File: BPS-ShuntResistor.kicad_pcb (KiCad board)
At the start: 2 copper layers, 40.1 x 35.1 mm, 15 parts, among them J3 Amp_Conn

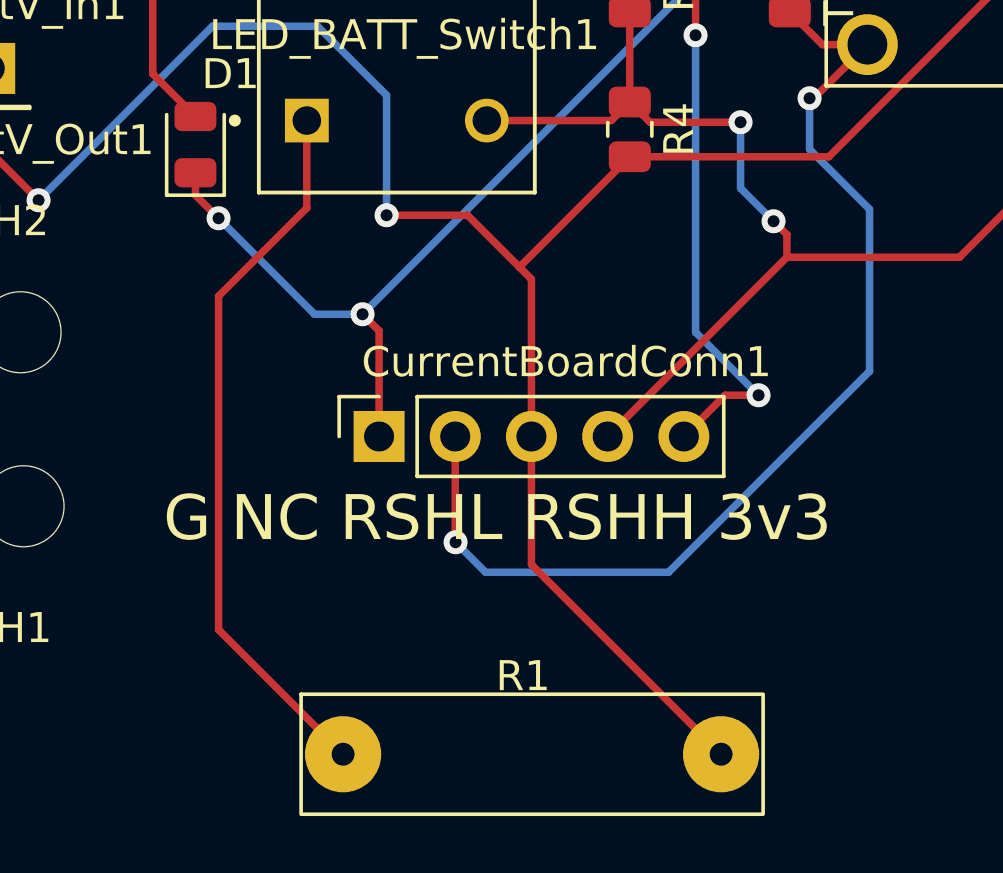
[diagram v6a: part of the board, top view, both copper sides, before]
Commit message: Updated BOM csv with approximate prices and potential Mouser lists
Ignore PCB update, footprint for 1x5 connector not decided
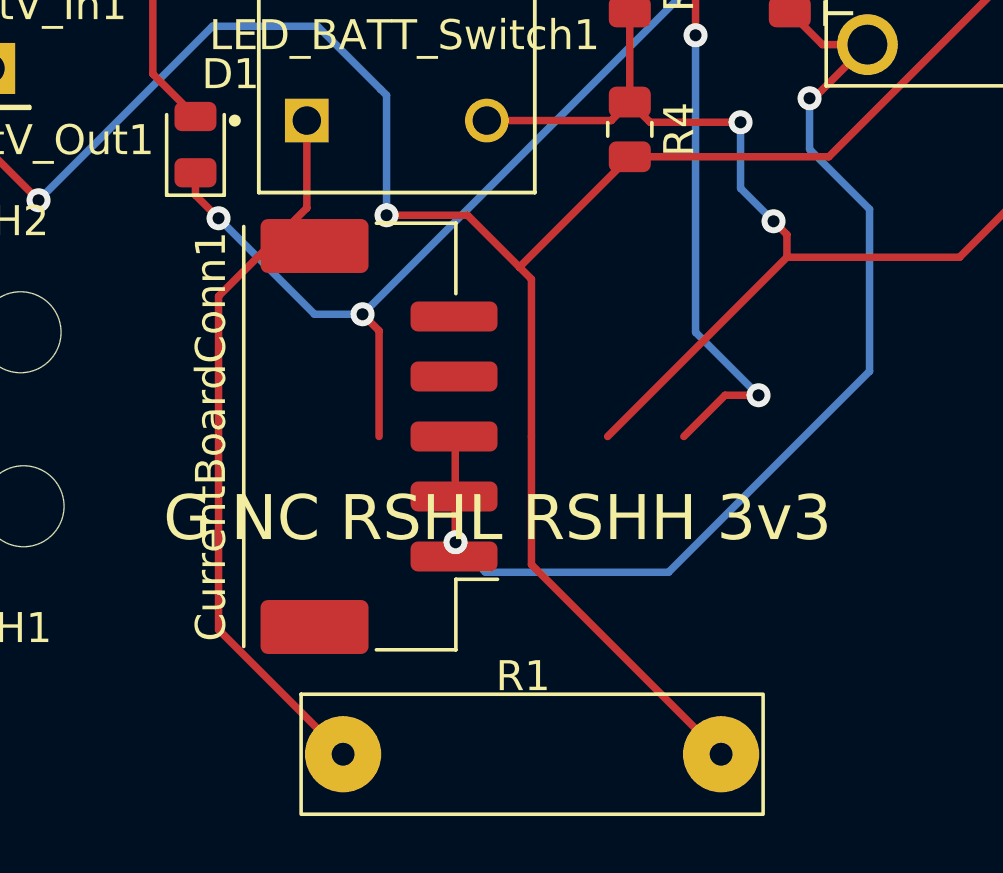
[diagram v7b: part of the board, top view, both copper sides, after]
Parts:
- CurrentBoardConn1: value Conn_01x05_Female -> Conn_01x05_Male; footprint Connector_PinSocket_2.54mm:PinSocket_1x05_P2.54mm_Vertical -> Connector_Molex:Molex_CLIK-Mate_502443-0570_1x05-1MP_P2.00mm_Vertical
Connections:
- CurrentBoardConn1 pad 1: GND -> ETS
- CurrentBoardConn1 pad 2: ETS -> RSHL
- CurrentBoardConn1 pad 3: RSHL -> RSHH
- CurrentBoardConn1 pad 4: RSHH -> +3V3
- CurrentBoardConn1 pad 5: +3V3 -> GND
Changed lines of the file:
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@@
   (net 4 "RSHL")
   (net 5 "RSHH")
-  (net 6 "Net-(R1-Pad1)")
-  (net 7 "Net-(R2-Pad2)")
+  (net 6 "Net-(LED_BATT_Switch1-Pad1)")
+  (net 7 "Net-(LED_BATT_Switch1-Pad3)")
   (net 8 "+3V3")
   (net 9 "Net-(R3-Pad1)")
@@
       (net 2 "Net-(D1-Pad2)") (pintype "passive"))
     (pad "2" smd roundrect (at 0.9125 0) (size 1.025 1.4) (layers "F.Cu" "F.Paste" "F.Mask") (roundrect_rratio 0.243902)
-      (net 7 "Net-(R2-Pad2)") (pintype "passive"))
+      (net 7 "Net-(LED_BATT_Switch1-Pad3)") (pintype "passive"))
     (model "${KICAD6_3DMODEL_DIR}/Resistor_SMD.3dshapes/R_0805_2012Metric.wrl"
       (offset (xyz 0 0 0))
@@
     (fp_circle (center -5.4 2.5) (end -5.3 2.5) (layer "F.Fab") (width 0.2) (fill none))
     (pad "1" thru_hole rect (at -3 2.5) (size 1.458 1.458) (drill 0.95) (layers *.Cu *.Mask)
-      (net 6 "Net-(R1-Pad1)") (pinfunction "1") (pintype "passive"))
+      (net 6 "Net-(LED_BATT_Switch1-Pad1)") (pinfunction "1") (pintype "passive"))
     (pad "2" thru_hole circle (at 3 2.5) (size 1.458 1.458) (drill 0.95) (layers *.Cu *.Mask)
       (net 5 "RSHH") (pinfunction "2") (pintype "passive"))
     (pad "3" thru_hole circle (at -3 -2.5) (size 1.458 1.458) (drill 0.95) (layers *.Cu *.Mask)
-      (net 7 "Net-(R2-Pad2)") (pinfunction "3") (pintype "passive"))
+      (net 7 "Net-(LED_BATT_Switch1-Pad3)") (pinfunction "3") (pintype "passive"))
     (pad "4" thru_hole circle (at 3 -2.5) (size 1.458 1.458) (drill 0.95) (layers *.Cu *.Mask)
       (net 8 "+3V3") (pinfunction "4") (pintype "passive"))
   )
-  (footprint "Connector_PinSocket_2.54mm:PinSocket_1x05_P2.54mm_Vertical" (layer "F.Cu")
+  (footprint "Connector_Molex:Molex_CLIK-Mate_502443-0570_1x05-1MP_P2.00mm_Vertical" (layer "F.Cu")
     (at 81.05 72.975 90)
-    (descr "Through hole straight socket strip, 1x05, 2.54mm pitch, single row (from Kicad 4.0.7), script generated")
-    (tags "Through hole socket strip THT 1x05 2.54mm single row")
-    (property "Sheetfile" "BPS-ShuntResistor.kicad_sch")
-    (property "Sheetname" "")
-    (attr through_hole)
-    (fp_text reference "CurrentBoardConn1" (at 2.475 6.25 180) (layer "F.SilkS")
-      (effects (font (size 1 1) (thickness 0.15)))
-    )
-    (fp_text value "Conn_01x05_Female" (at 0 12.93 90) (layer "F.Fab")
-      (effects (font (size 1 1) (thickness 0.15)))
-    )
-    (fp_text user "${REFERENCE}" (at 0 5.08) (layer "F.Fab")
-      (effects (font (size 1 1) (thickness 0.15)))
-    )
-    (fp_line (start 1.33 1.27) (end 1.33 11.49) (layer "F.SilkS") (width 0.12))
-    (fp_line (start -1.33 1.27) (end 1.33 1.27) (layer "F.SilkS") (width 0.12))
-    (fp_line (start 0 -1.33) (end 1.33 -1.33) (layer "F.SilkS") (width 0.12))
-    (fp_line (start 1.33 -1.33) (end 1.33 0) (layer "F.SilkS") (width 0.12))
-    (fp_line (start -1.33 1.27) (end -1.33 11.49) (layer "F.SilkS") (width 0.12))
-    (fp_line (start -1.33 11.49) (end 1.33 11.49) (layer "F.SilkS") (width 0.12))
-    (fp_line (start 1.75 -1.8) (end 1.75 11.9) (layer "F.CrtYd") (width 0.05))
-    (fp_line (start 1.75 11.9) (end -1.8 11.9) (layer "F.CrtYd") (width 0.05))
-    (fp_line (start -1.8 11.9) (end -1.8 -1.8) (layer "F.CrtYd") (width 0.05))
-    (fp_line (start -1.8 -1.8) (end 1.75 -1.8) (layer "F.CrtYd") (width 0.05))
-    (fp_line (start 1.27 -0.635) (end 1.27 11.43) (layer "F.Fab") (width 0.1))
-    (fp_line (start -1.27 11.43) (end -1.27 -1.27) (layer "F.Fab") (width 0.1))
-    (fp_line (start 1.27 11.43) (end -1.27 11.43) (layer "F.Fab") (width 0.1))
-    (fp_line (start -1.27 -1.27) (end 0.635 -1.27) (layer "F.Fab") (width 0.1))
-    (fp_line (start 0.635 -1.27) (end 1.27 -0.635) (layer "F.Fab") (width 0.1))
-    (pad "1" thru_hole rect (at 0 0 90) (size 1.7 1.7) (drill 1) (layers *.Cu *.Mask)
-      (net 1 "GND") (pinfunction "Pin_1") (pintype "passive"))
-    (pad "2" thru_hole oval (at 0 2.54 90) (size 1.7 1.7) (drill 1) (layers *.Cu *.Mask)
-      (net 3 "ETS") (pinfunction "Pin_2") (pintype "passive"))
-    (pad "3" thru_hole oval (at 0 5.08 90) (size 1.7 1.7) (drill 1) (layers *.Cu *.Mask)
-      (net 4 "RSHL") (pinfunction "Pin_3") (pintype "passive"))
-    (pad "4" thru_hole oval (at 0 7.62 90) (size 1.7 1.7) (drill 1) (layers *.Cu *.Mask)
-      (net 5 "RSHH") (pinfunction "Pin_4") (pintype "passive"))
-    (pad "5" thru_hole oval (at 0 10.16 90) (size 1.7 1.7) (drill 1) (layers *.Cu *.Mask)
-      (net 8 "+3V3") (pinfunction "Pin_5") (pintype "passive"))
-    (model "${KICAD6_3DMODEL_DIR}/Connector_PinSocket_2.54mm.3dshapes/PinSocket_1x05_P2.54mm_Vertical.wrl"
+    (descr "Molex CLIK-Mate series connector, 502443-0570 (http://www.molex.com/pdm_docs/sd/5024430270_sd.pdf), generated with kicad-footprint-generator")
+    (tags "connector Molex CLIK-Mate side entry")
+    (property "Sheetfile" "BPS-ShuntResistor.kicad_sch")
+    (property "Sheetname" "")
+    (attr smd)
+    (fp_text reference "CurrentBoardConn1" (at 0 -5.6 90) (layer "F.SilkS")
+      (effects (font (size 1 1) (thickness 0.15)))
+    )
+    (fp_text value "Conn_01x05_Male" (at 0 5.15 90) (layer "F.Fab")
+      (effects (font (size 1 1) (thickness 0.15)))
+    )
+    (fp_text user "${REFERENCE}" (at 0 -0.98 90) (layer "F.Fab")
+      (effects (font (size 1 1) (thickness 0.15)))
+    )
+    (fp_line (start -4.76 2.56) (end -4.76 3.95) (layer "F.SilkS") (width 0.12))
+    (fp_line (start 7.11 -0.09) (end 7.11 2.56) (layer "F.SilkS") (width 0.12))
+    (fp_line (start 7.11 2.56) (end 4.76 2.56) (layer "F.SilkS") (width 0.12))
+    (fp_line (start -7.11 -0.09) (end -7.11 2.56) (layer "F.SilkS") (width 0.12))
+    (fp_line (start -7.11 2.56) (end -4.76 2.56) (layer "F.SilkS") (width 0.12))
+    (fp_line (start -7 -4.51) (end 7 -4.51) (layer "F.SilkS") (width 0.12))
+    (fp_line (start -7.75 -4.9) (end -7.75 4.45) (layer "F.CrtYd") (width 0.05))
+    (fp_line (start 7.75 4.45) (end 7.75 -4.9) (layer "F.CrtYd") (width 0.05))
+    (fp_line (start 7.75 -4.9) (end -7.75 -4.9) (layer "F.CrtYd") (width 0.05))
+    (fp_line (start -7.75 4.45) (end 7.75 4.45) (layer "F.CrtYd") (width 0.05))
+    (fp_line (start -7 -4.4) (end 7 -4.4) (layer "F.Fab") (width 0.1))
+    (fp_line (start -7 2.45) (end -7 -4.4) (layer "F.Fab") (width 0.1))
+    (fp_line (start -4.5 2.45) (end -4 1.742893) (layer "F.Fab") (width 0.1))
+    (fp_line (start 7 2.45) (end 7 -4.4) (layer "F.Fab") (width 0.1))
+    (fp_line (start -4 1.742893) (end -3.5 2.45) (layer "F.Fab") (width 0.1))
+    (fp_line (start -7 2.45) (end 7 2.45) (layer "F.Fab") (width 0.1))
+    (pad "1" smd roundrect (at -4 2.5 90) (size 1 2.9) (layers "F.Cu" "F.Paste" "F.Mask") (roundrect_rratio 0.25)
+      (net 3 "ETS") (pinfunction "Pin_1") (pintype "passive"))
+    (pad "2" smd roundrect (at -2 2.5 90) (size 1 2.9) (layers "F.Cu" "F.Paste" "F.Mask") (roundrect_rratio 0.25)
+      (net 4 "RSHL") (pinfunction "Pin_2") (pintype "passive"))
+    (pad "3" smd roundrect (at 0 2.5 90) (size 1 2.9) (layers "F.Cu" "F.Paste" "F.Mask") (roundrect_rratio 0.25)
+      (net 5 "RSHH") (pinfunction "Pin_3") (pintype "passive"))
+    (pad "4" smd roundrect (at 2 2.5 90) (size 1 2.9) (layers "F.Cu" "F.Paste" "F.Mask") (roundrect_rratio 0.25)
+      (net 8 "+3V3") (pinfunction "Pin_4") (pintype "passive"))
+    (pad "5" smd roundrect (at 4 2.5 90) (size 1 2.9) (layers "F.Cu" "F.Paste" "F.Mask") (roundrect_rratio 0.25)
+      (net 1 "GND") (pinfunction "Pin_5") (pintype "passive"))
+    (pad "MP" smd roundrect (at -6.35 -2.15 90) (size 1.8 3.6) (layers "F.Cu" "F.Paste" "F.Mask") (roundrect_rratio 0.138889))
+    (pad "MP" smd roundrect (at 6.35 -2.15 90) (size 1.8 3.6) (layers "F.Cu" "F.Paste" "F.Mask") (roundrect_rratio 0.138889))
+    (model "${KICAD6_3DMODEL_DIR}/Connector_Molex.3dshapes/Molex_CLIK-Mate_502443-0570_1x05-1MP_P2.00mm_Vertical.wrl"
       (offset (xyz 0 0 0))
       (scale (xyz 1 1 1))
@@
     (fp_rect (start -7.4 -2) (end 8 2) (layer "F.SilkS") (width 0.12) (fill none))
     (pad "1" thru_hole circle (at -6 0) (size 2.54 2.54) (drill 0.762) (layers *.Cu *.Mask)
-      (net 6 "Net-(R1-Pad1)") (pintype "passive"))
+      (net 6 "Net-(LED_BATT_Switch1-Pad1)") (pintype "passive"))
     (pad "2" thru_hole circle (at 6.6 0) (size 2.54 2.54) (drill 0.762) (layers *.Cu *.Mask)
       (net 4 "RSHL") (pintype "passive"))

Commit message: Working on new layout
Kind of messy
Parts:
- CurrentBoardConn1: footprint Connector_Molex:Molex_CLIK-Mate_502443-0570_1x05-1MP_P2.00mm_Vertical -> Connector_PinHeader_2.54mm:PinHeader_1x05_P2.54mm_Vertical
- LOGO1, LOGO2: moved to F.Cu
- moved H1 94.0 mm to (153.9, 116.0)
- moved TestV_In1 68.5 mm to (129.2, 87.0)
- moved R2 66.2 mm to (133.1, 87.9), turned to 90 degrees
- moved LED_BATT_Switch1 65.6 mm to (140.0, 90.0)
- moved D1 65.0 mm to (133.1, 92.3)
- moved TH1 61.1 mm to (147.6, 88.5)
- moved J3 60.4 mm to (153.0, 87.5)
- moved H2 60.3 mm to (125.0, 92.1)
- moved CurrentBoardConn1 58.2 mm to (131.7, 101.6)
- moved TestV_Out1 57.9 mm to (119.7, 86.9)
- moved R1 57.5 mm to (137.2, 109.6), turned to 180 degrees
- moved LOGO2 56.4 mm to (150.5, 103.1), turned to 0 degrees
- moved R4 55.1 mm to (123.6, 106.0)
- moved LOGO1 54.9 mm to (126.3, 115.7), turned to 0 degrees
- moved R3 53.2 mm to (123.6, 98.7)
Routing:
- net RSHL: track 70.3 -> 40.8 mm, vias 2 -> 0
- net RSHH: track 39.6 -> 48.7 mm
- net Net-(R3-Pad1): track 22.3 -> 14.2 mm, vias 1 -> 0
- net +3V3: track 27.9 -> 20.7 mm, vias 2 -> 0
- net Net-(LED_BATT_Switch1-Pad1): track 24.1 -> 19.7 mm, vias 0 -> 2
- net Net-(D1-Pad2): track 5.75 -> 2.53 mm
- net ETS: track 36.2 -> 34.1 mm
- net GND: track 36.3 -> 35.4 mm
- net Net-(LED_BATT_Switch1-Pad3): track 3.43 -> 4.08 mm
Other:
- board text removed: "G NC RSHL RSHH 3v3"
